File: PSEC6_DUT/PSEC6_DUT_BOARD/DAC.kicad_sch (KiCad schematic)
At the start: 4 parts, among them U10 DAC8411IDCKT

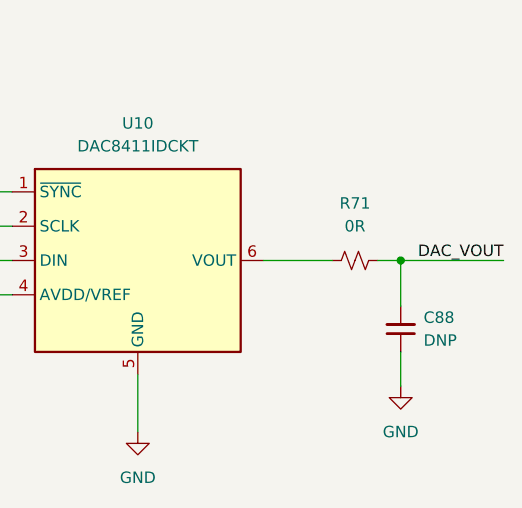
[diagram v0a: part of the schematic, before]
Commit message: Many Updates
Starting new power sequence and implementing KR260 PS circuitry.
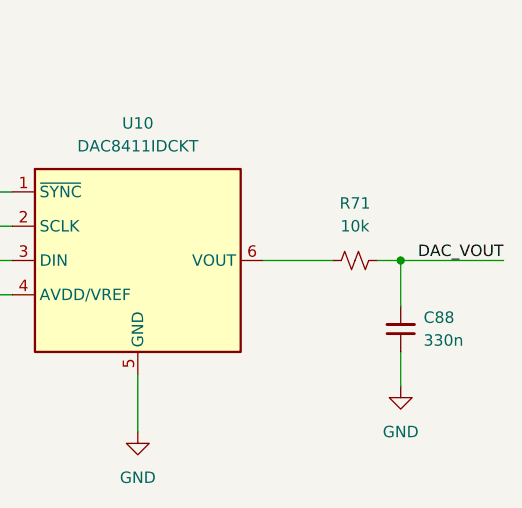
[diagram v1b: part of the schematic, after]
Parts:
- C88: value DNP -> 330n
- R71: value 0R -> 10k
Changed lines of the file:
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@@
 			)
 		)
-		(property "Value" "0R"
+		(property "Value" "10k"
 			(at 208.28 49.53 90)
 			(show_name no)
@@
 			)
 		)
-		(property "Value" "DNP"
+		(property "Value" "330n"
 			(at 215.9 62.2235 0)
 			(show_name no)
